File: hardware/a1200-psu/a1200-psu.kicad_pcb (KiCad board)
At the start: 2 copper layers, 147 x 76 mm, 7 parts, among them Q1 BC327, Q2 BC327, Q4 P2N60, U1 PC817, U2 TL431D, U3 UC3844_DIP8

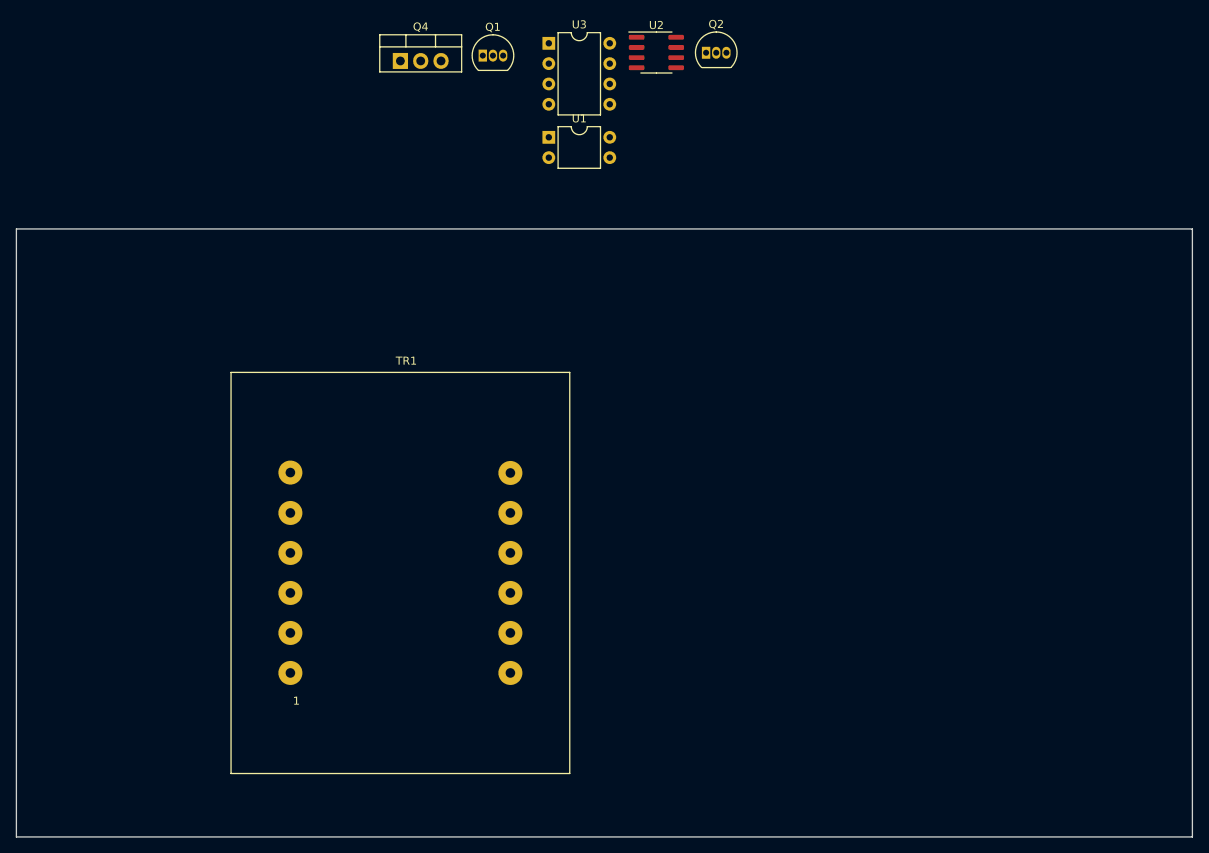
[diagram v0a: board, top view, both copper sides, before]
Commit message: Fixed R values and added to PCB
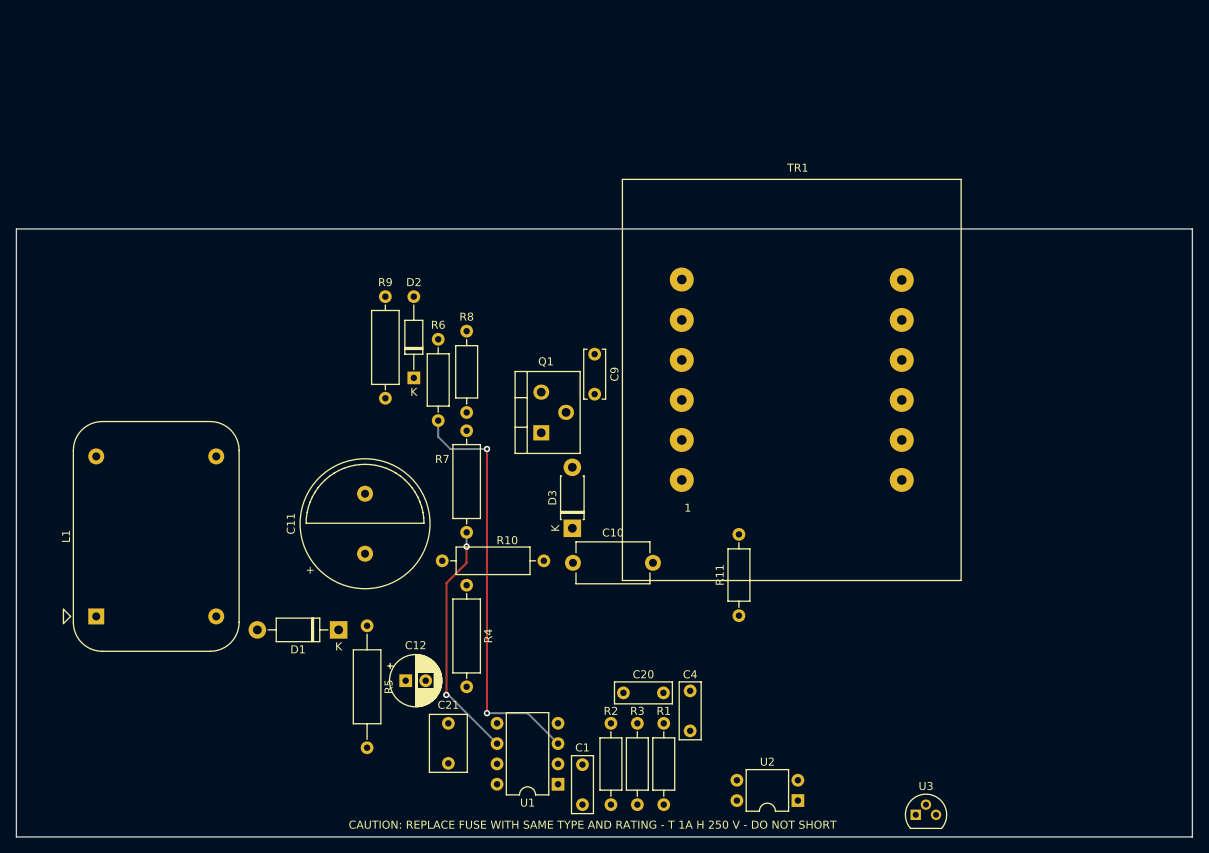
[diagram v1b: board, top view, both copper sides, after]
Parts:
- removed Q2: BC327, Package_TO_SOT_THT:TO-92_Inline
- removed Q4: P2N60, Package_TO_SOT_THT:TO-220-3_Vertical
- removed the U2 at (152.8, 30.4)
- added C1: 10nF, Capacitor_THT:C_Rect_L7.0mm_W2.5mm_P5.00mm, F.Cu at (143.5, 119.5)
- added C10: 10n, Capacitor_THT:C_Disc_D9.0mm_W5.0mm_P10.00mm, F.Cu at (142.3, 94.2)
- added C11: 33uF, Capacitor_THT:C_Radial_D16.0mm_H31.5mm_P7.50mm, F.Cu at (116.3, 93.1)
- added C12: 47uF, Capacitor_THT:CP_Radial_D6.3mm_P2.50mm, F.Cu at (121.4, 109.0)
- added C20: 1nF, Capacitor_THT:C_Rect_L7.0mm_W2.5mm_P5.00mm, F.Cu at (148.6, 110.5)
- added C21: 470pF, Capacitor_THT:C_Rect_L7.0mm_W4.5mm_P5.00mm, F.Cu at (126.7, 119.3)
- added C4: 10nF, Capacitor_THT:C_Rect_L7.0mm_W2.5mm_P5.00mm, F.Cu at (157.0, 115.2)
- added C9: 220pF, Capacitor_THT:C_Disc_D6.0mm_W2.5mm_P5.00mm, F.Cu at (145.0, 68.2)
- added D1: 1N4007, Diode_THT:D_DO-41_SOD81_P10.16mm_Horizontal, F.Cu at (113.0, 102.6)
- added D2: 1N4742A, Diode_THT:D_DO-35_SOD27_P10.16mm_Horizontal, F.Cu at (122.4, 71.1)
- added D3: BYV26E, Diode_THT:D_DO-41_SOD81_P7.62mm_Horizontal, F.Cu at (142.2, 89.9)
- added L1: 47mH, Filter:Filter_FILTERCON_1FPxx, F.Cu at (82.7, 100.9)
- added R1: 680R, Resistor_THT:R_Axial_DIN0207_L6.3mm_D2.5mm_P10.16mm_Horizontal, F.Cu at (153.7, 114.3)
- added R10: 100k, Resistor_THT:R_Axial_DIN0309_L9.0mm_D3.2mm_P12.70mm_Horizontal, F.Cu at (126.0, 94.0)
- added R11: 20k, Resistor_THT:R_Axial_DIN0207_L6.3mm_D2.5mm_P10.16mm_Horizontal, F.Cu at (163.1, 100.8)
- added R2: 240k, Resistor_THT:R_Axial_DIN0207_L6.3mm_D2.5mm_P10.16mm_Horizontal, F.Cu at (147.1, 124.5)
- added R3: 25k5, Resistor_THT:R_Axial_DIN0207_L6.3mm_D2.5mm_P10.16mm_Horizontal, F.Cu at (150.4, 124.5)
- added R4: 821k, Resistor_THT:R_Axial_DIN0309_L9.0mm_D3.2mm_P12.70mm_Horizontal, F.Cu at (129.0, 97.0)
- added R5: 68k, Resistor_THT:R_Axial_DIN0309_L9.0mm_D3.2mm_P15.24mm_Horizontal, F.Cu at (116.6, 102.1)
- added R6: 460R, Resistor_THT:R_Axial_DIN0207_L6.3mm_D2.5mm_P10.16mm_Horizontal, F.Cu at (125.5, 76.5)
- added R7: 150R, Resistor_THT:R_Axial_DIN0309_L9.0mm_D3.2mm_P12.70mm_Horizontal, F.Cu at (129.0, 77.7)
- added R8: 20k, Resistor_THT:R_Axial_DIN0207_L6.3mm_D2.5mm_P10.16mm_Horizontal, F.Cu at (129.0, 75.4)
- added R9: 1R, Resistor_THT:R_Axial_DIN0309_L9.0mm_D3.2mm_P12.70mm_Horizontal, F.Cu at (118.9, 73.7)
- added U1: UC3844_DIP8, Package_DIP:DIP-8_W7.62mm, F.Cu at (140.5, 121.9)
- Q1: value BC327 -> P2N60; footprint Package_TO_SOT_THT:TO-92_Inline -> Amiga 1200:TO-220-3_Vertical_Staggered
- U3: value UC3844_DIP8 -> TL431D; footprint Package_DIP:DIP-8_W7.62mm -> Package_TO_SOT_THT:TO-92L
- moved U3 106.8 mm to (185.2, 125.7)
- moved U2 88.6 mm to (170.4, 124.0), turned to 180 degrees
- moved TR1 54.5 mm to (155.9, 83.9)
- moved Q1 47.7 mm to (138.4, 78.0), turned to 90 degrees
- renumbered U1 to U2
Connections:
- net Net-(C12-Pad1) renamed +5V
- Q1 pad 1: Net-(D1-Pad2) -> Net-(Q1-Pad1)
- Q1 pad 2: Net-(C1-Pad2) (its old number) -> Net-(C9-Pad2)
- TR1 pad 10: GND -> Net-(D8-Pad2)
- TR1 pad 3: Net-(C9-Pad1) (its old number) -> Net-(C9-Pad2)
- TR1 pad 6: Net-(C5-Pad1) -> GNDD
- U2 pad 3: Net-(D1-Pad2) -> GNDD
- U3 pad 1: unconnected-(U3-Pad1) -> Net-(C19-Pad1)
- U3 pad 2: unconnected-(U3-Pad2) -> GND
- U3 pad 3: unconnected-(U3-Pad3) -> GND
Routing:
- net Net-(C21-Pad1): track 0.00 -> 52.2 mm, vias 0 -> 2
- net Net-(R7-Pad2): track 0.00 -> 30.2 mm, vias 0 -> 2
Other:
- board text added: "!! WIP !!"
- board text added: "+"
- board text added: "AC/DC line voltage"
- board text added: "CAUTION: REPLACE FUSE WITH SAME TYPE AND RATING - T 1A H 250 V - DO NOT SHORT"
- board text added: "DC stepped down"
- board text added: "TODO: Change footprint to 22mm"
- board text removed: "TODO: new footprint 22mm"

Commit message: Add transformer footprint
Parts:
- TR1: footprint Transformer_THT:Transformer_CHK_EI48-8VA_Neutral -> Amiga 1200:Transformer
- moved TR1 16.5 mm to (166.4, 71.1)
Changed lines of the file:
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@@
     )
   )
-  (footprint "Transformer_THT:Transformer_CHK_EI48-8VA_Neutral" (layer "F.Cu")
-    (at 155.922 83.874)
+  (footprint "Amiga 1200:Transformer" (layer "F.Cu")
+    (at 166.37 71.12)
     (descr "Trafo, Printtrafo, CHK, EI48, 8VA, neutral, http://www.eratransformers.com/product-detail/18")
     (tags "Trafo Printtrafo CHK EI48 8VA neutral ")
@@
     (property "Value 9-12" "0mH 2.41 Ω")
     (attr through_hole)
-    (fp_text reference "TR1" (at 14.5 -39) (layer "F.SilkS")
+    (fp_text reference "TR1" (at 8.636 -17.062) (layer "F.SilkS")
       (effects (font (size 1 1) (thickness 0.15)))
     )
-    (fp_text value "A1200-PSU-TR" (at 14.3 -12.6 90) (layer "F.Fab")
+    (fp_text value "A1200-PSU-TR" (at 0 -20.32 180) (layer "F.Fab")
       (effects (font (size 1 1) (thickness 0.15)))
     )
-    (fp_text user "1" (at 0.75 3.5) (layer "F.SilkS")
+    (fp_text user "${REFERENCE}" (at 0.1 -18.02 180) (layer "F.Fab")
       (effects (font (size 1 1) (thickness 0.15)))
     )
-    (fp_text user "7" (at 27.75 -28.5) (layer "F.Fab")
-      (effects (font (size 1 1) (thickness 0.15)))
-    )
-    (fp_text user "12" (at 27.75 4.5) (layer "F.Fab")
-      (effects (font (size 1 1) (thickness 0.15)))
-    )
-    (fp_text user "${REFERENCE}" (at 12 -12.5 90) (layer "F.Fab")
-      (effects (font (size 1 1) (thickness 0.15)))
-    )
-    (fp_text user "6" (at -0.25 -29.5) (layer "F.Fab")
-      (effects (font (size 1 1) (thickness 0.15)))
-    )
-    (fp_line (start -7.42 -37.57) (end -7.42 12.57) (layer "F.SilkS") (width 0.12))
-    (fp_line (start 34.92 12.57) (end -7.42 12.57) (layer "F.SilkS") (width 0.12))
-    (fp_line (start -7.42 -37.57) (end 34.92 -37.57) (layer "F.SilkS") (width 0.12))
-    (fp_line (start 34.92 12.57) (end 34.92 -37.57) (layer "F.SilkS") (width 0.12))
-    (fp_line (start 35.05 12.7) (end 35.05 -37.7) (layer "F.CrtYd") (width 0.05))
-    (fp_line (start 35.05 12.7) (end -7.55 12.7) (layer "F.CrtYd") (width 0.05))
-    (fp_line (start -7.55 -37.7) (end 35.05 -37.7) (layer "F.CrtYd") (width 0.05))
-    (fp_line (start -7.55 -37.7) (end -7.55 12.7) (layer "F.CrtYd") (width 0.05))
-    (fp_line (start 34.8 -37.45) (end 34.8 12.45) (layer "F.Fab") (width 0.1))
-    (fp_line (start 34.8 12.45) (end -7.3 12.45) (layer "F.Fab") (width 0.1))
-    (fp_line (start -7.3 12.45) (end -7.3 -37.45) (layer "F.Fab") (width 0.1))
-    (fp_line (start -7.3 -37.45) (end 34.8 -37.45) (layer "F.Fab") (width 0.1))
-    (pad "1" thru_hole circle (at 0 0) (size 3 3) (drill 1.2) (layers *.Cu *.Mask)
+    (fp_line (start -13.381 -15.632) (end -13.368 15.697) (layer "F.SilkS") (width 0.12))
+    (fp_line (start 14.332 15.7) (end -13.368 15.697) (layer "F.SilkS") (width 0.12))
+    (fp_line (start 14.332 15.7) (end 14.332 -15.63) (layer "F.SilkS") (width 0.12))
+    (fp_line (start -13.381 -15.632) (end 14.332 -15.63) (layer "F.SilkS") (width 0.12))
+    (fp_circle (center -12.191 14.54) (end -11.83179 14.54) (layer "F.SilkS") (width 0.12) (fill solid))
+    (fp_rect (start -10.16 -12.62) (end 11.303 12.399) (layer "Dwgs.User") (width 0.12) (fill none))
+    (fp_line (start -13.511 -15.762) (end 14.462 -15.76) (layer "F.CrtYd") (width 0.05))
+    (fp_line (start -13.511 -15.762) (end -13.498 15.827) (layer "F.CrtYd") (width 0.05))
+    (fp_line (start 14.462 15.79) (end 14.462 -15.76) (layer "F.CrtYd") (width 0.05))
+    (fp_line (start 14.462 15.79) (end -13.498 15.827) (layer "F.CrtYd") (width 0.05))
+    (fp_line (start -13.261 -15.512) (end 14.212 -15.51) (layer "F.Fab") (width 0.1))
+    (fp_line (start -13.248 15.577) (end -13.261 -15.512) (layer "F.Fab") (width 0.1))
+    (fp_line (start 14.212 15.58) (end -13.248 15.577) (layer "F.Fab") (width 0.1))
+    (fp_line (start 14.212 -15.51) (end 14.212 15.58) (layer "F.Fab") (width 0.1))
+    (pad "1" thru_hole circle (at -10.287 12.399) (size 3 3) (drill 1.2) (layers *.Cu *.Mask)
       (net 6 "Net-(C10-Pad1)") (pintype "passive"))
-    (pad "2" thru_hole circle (at 0 -5) (size 3 3) (drill 1.2) (layers *.Cu *.Mask))
-    (pad "3" thru_hole circle (at 0 -10) (size 3 3) (drill 1.2) (layers *.Cu *.Mask)
+    (pad "2" thru_hole circle (at -10.16 7.46) (size 3 3) (drill 1.2) (layers *.Cu *.Mask))
+    (pad "3" thru_hole circle (at -10.16 2.46) (size 3 3) (drill 1.2) (layers *.Cu *.Mask)
       (net 2 "Net-(C9-Pad2)") (pintype "passive"))
-    (pad "4" thru_hole circle (at 0 -15) (size 3 3) (drill 1.2) (layers *.Cu *.Mask))
-    (pad "5" thru_hole circle (at 0 -20) (size 3 3) (drill 1.2) (layers *.Cu *.Mask)
+    (pad "4" thru_hole circle (at -10.16 -2.54) (size 3 3) (drill 1.2) (layers *.Cu *.Mask))
+    (pad "5" thru_hole circle (at -10.16 -7.54) (size 3 3) (drill 1.2) (layers *.Cu *.Mask)
       (net 19 "Net-(R11-Pad2)") (pintype "passive"))
-    (pad "6" thru_hole circle (at 0 -25.05) (size 3 3) (drill 1.2) (layers *.Cu *.Mask)
+    (pad "6" thru_hole circle (at -10.16 -12.62) (size 3 3) (drill 1.2) (layers *.Cu *.Mask)
       (net 8 "GNDD") (pintype "passive"))
-    (pad "7" thru_hole circle (at 27.5 -25) (size 3 3) (drill 1.2) (layers *.Cu *.Mask)
+    (pad "7" thru_hole circle (at 11.303 -12.62) (size 3 3) (drill 1.2) (layers *.Cu *.Mask)
       (net 10 "Net-(D7-Pad1)") (pintype "passive"))
-    (pad "8" thru_hole circle (at 27.5 -20) (size 3 3) (drill 1.2) (layers *.Cu *.Mask)
+    (pad "8" thru_hole circle (at 11.303 -7.54) (size 3 3) (drill 1.2) (layers *.Cu *.Mask)
       (net 13 "GND") (pintype "passive"))
-    (pad "9" thru_hole circle (at 27.5 -15) (size 3 3) (drill 1.2) (layers *.Cu *.Mask)
+    (pad "9" thru_hole circle (at 11.303 -2.54) (size 3 3) (drill 1.2) (layers *.Cu *.Mask)
       (net 13 "GND") (pintype "passive"))
-    (pad "10" thru_hole circle (at 27.5 -10) (size 3 3) (drill 1.2) (layers *.Cu *.Mask)
+    (pad "10" thru_hole circle (at 11.303 2.46) (size 3 3) (drill 1.2) (layers *.Cu *.Mask)
       (net 14 "Net-(D8-Pad2)") (pintype "passive"))
-    (pad "11" thru_hole circle (at 27.5 -5) (size 3 3) (drill 1.2) (layers *.Cu *.Mask)
+    (pad "11" thru_hole circle (at 11.303 7.46) (size 3 3) (drill 1.2) (layers *.Cu *.Mask)
       (net 11 "Net-(C15-Pad1)") (pintype "passive"))
-    (pad "12" thru_hole circle (at 27.5 0) (size 3 3) (drill 1.2) (layers *.Cu *.Mask)
+    (pad "12" thru_hole circle (at 11.303 12.399) (size 3 3) (drill 1.2) (layers *.Cu *.Mask)
       (net 12 "Net-(D10-Pad2)") (pintype "passive"))
     (model "${KICAD6_3DMODEL_DIR}/Transformer_THT.3dshapes/Transformer_CHK_EI48-8VA_Neutral.wrl"
